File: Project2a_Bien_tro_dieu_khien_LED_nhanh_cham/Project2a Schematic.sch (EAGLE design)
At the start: 16 parts, among them U1 ARDUINOR3-BPLACE

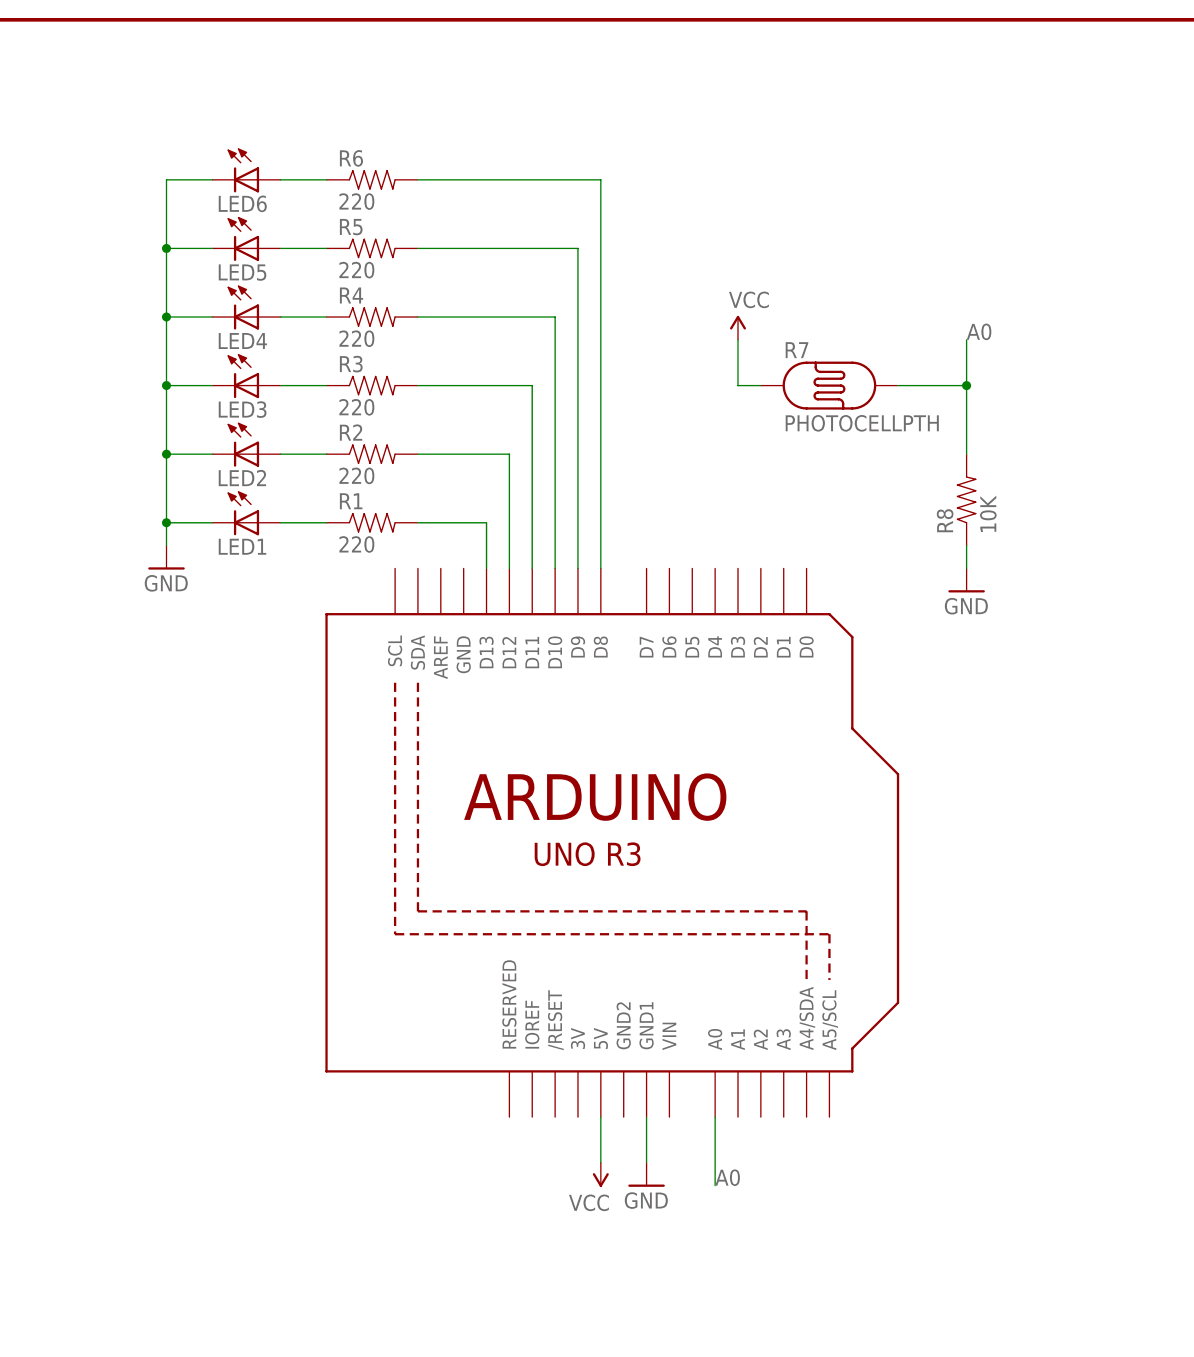
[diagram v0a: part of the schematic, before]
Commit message: Update schematic, breadboard cho nhieu projects.
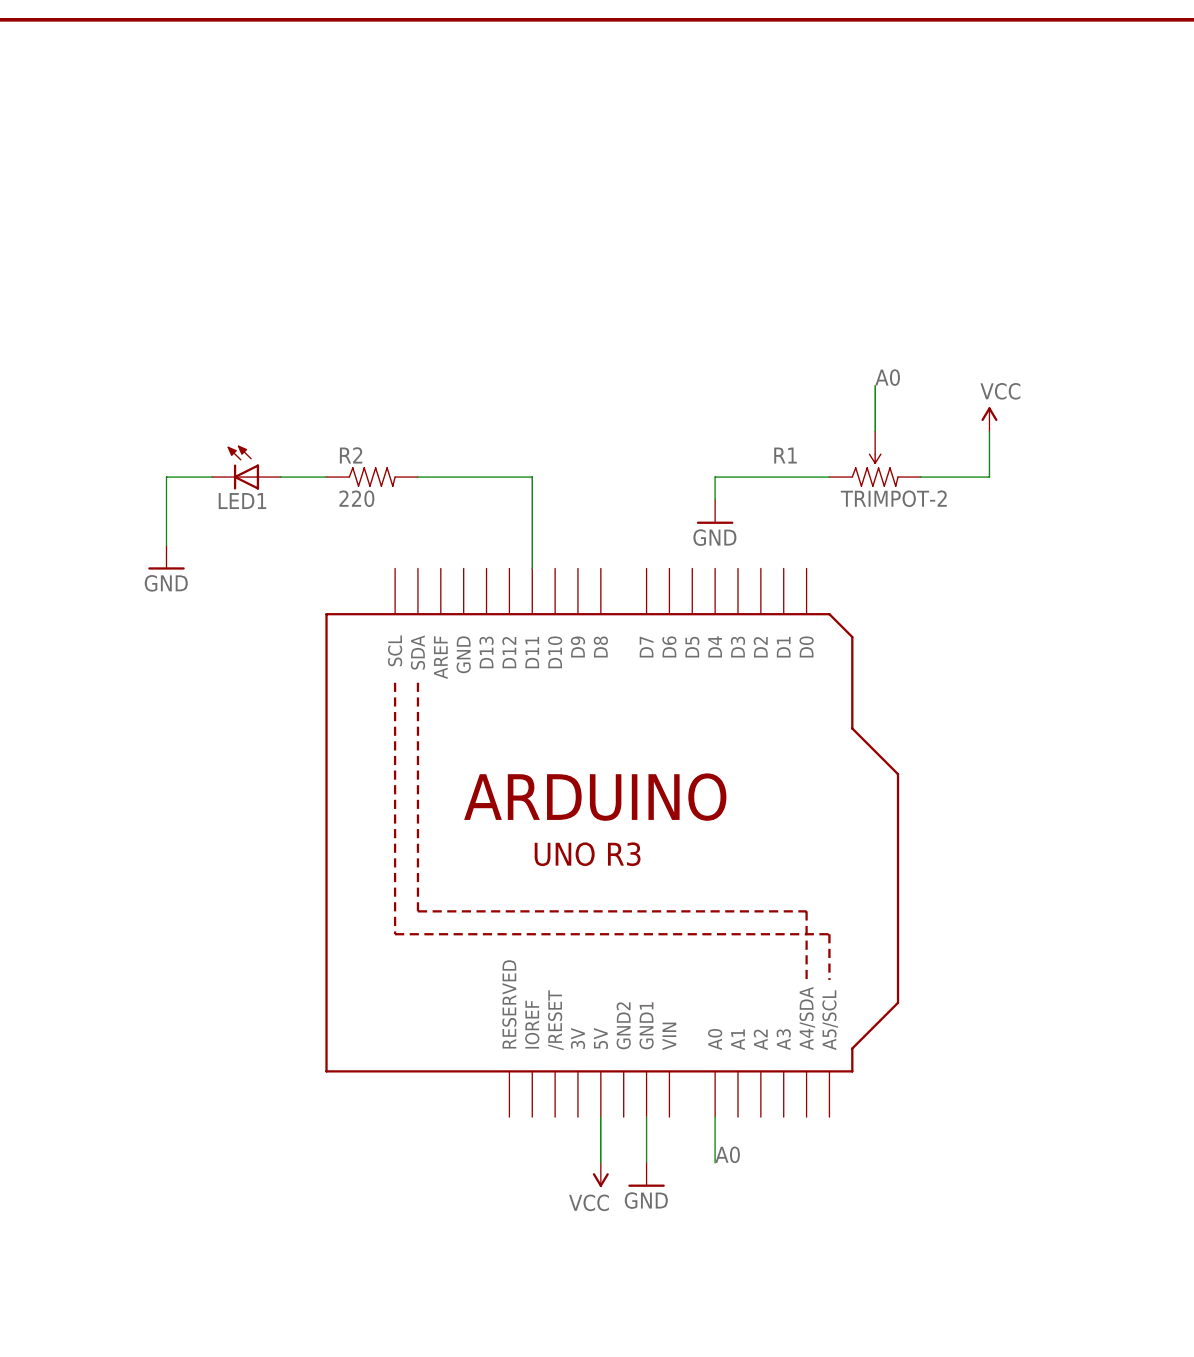
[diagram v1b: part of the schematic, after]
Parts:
- removed LED2, LED3, LED4, LED5, LED6: (no value), adafruit:LED
- removed R3, R4, R5, R6: 220, SparkFun-Passives:RESISTOR0402-RES
- removed R7: PHOTOCELLPTH, SparkFun-Sensors:PHOTOCELLPTH
- removed R8: 10K, SparkFun-Passives:RESISTOR0402-RES
- R1: value 220 -> TRIMPOT-2; device SparkFun-Passives:RESISTOR0402-RES -> SparkFun-Electromechanical:TRIMPOT-2
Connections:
- removed net N$10: LED5.A, R5.1
- removed net N$11: LED4.A, R4.1
- removed net N$12: R6.2, U1.D8
- removed net N$13: R5.2, U1.D9
- removed net N$14: R4.2, U1.D10
- removed net N$4: LED3.A, R3.1
- removed net N$5: LED2.A, R2.1
- removed net N$6: R3.2, U1.D11
- removed net N$7: R2.2, U1.D12
- removed net N$9: LED6.A, R6.1
- net A0: now also R1.WIPER; no longer R7.P$2, R8.2
- net GND: now also R1.CCW; no longer LED2.C, LED3.C, LED4.C, LED5.C, LED6.C, R8.1
- net N$1: now also R2.2, U1.D11; no longer R1.2, U1.D13
- net N$2: now also R2.1; no longer R1.1
- net VCC: now also R1.CW; no longer R7.P$1
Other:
- moved on the sheet: LED1, R2

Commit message: Thay doi schematic cua projects.
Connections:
- net A0 renamed N$3
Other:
- moved on the sheet: R1
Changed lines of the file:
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@@
 <?xml version="1.0" encoding="utf-8"?>
 <!DOCTYPE eagle SYSTEM "eagle.dtd">
-<eagle version="7.2.0">
+<eagle version="7.3.0">
 <drawing>
 <settings>
@@
 <setting verticaltext="up"/>
 </settings>
-<grid distance="0.1" unitdist="inch" unit="inch" style="dots" multiple="1" display="yes" altdistance="0.01" altunitdist="inch" altunit="inch"/>
+<grid distance="0.1" unitdist="inch" unit="inch" style="lines" multiple="1" display="yes" altdistance="0.01" altunitdist="inch" altunit="inch"/>
 <layers>
 <layer number="1" name="Top" color="4" fill="1" visible="no" active="no"/>
@@
 <instance part="LED1" gate="G$1" x="38.1" y="119.38" rot="R270"/>
 <instance part="GND2" gate="1" x="27.94" y="109.22"/>
-<instance part="GND3" gate="1" x="88.9" y="114.3"/>
-<instance part="SUPPLY2" gate="G$1" x="119.38" y="124.46"/>
+<instance part="GND3" gate="1" x="88.9" y="30.48"/>
+<instance part="SUPPLY2" gate="G$1" x="119.38" y="40.64"/>
 <instance part="FRAME1" gate="G$1" x="-33.02" y="-15.24"/>
 <instance part="FRAME1" gate="V" x="114.3" y="-15.24"/>
-<instance part="R1" gate="R?" x="106.68" y="119.38"/>
+<instance part="R1" gate="R?" x="106.68" y="35.56"/>
 </instances>
 <busses>
@@
 <segment>
 <pinref part="R1" gate="R?" pin="CW"/>
-<wire x1="111.76" y1="119.38" x2="119.38" y2="119.38" width="0.1524" layer="91"/>
+<wire x1="111.76" y1="35.56" x2="119.38" y2="35.56" width="0.1524" layer="91"/>
 <pinref part="SUPPLY2" gate="G$1" pin="VCC"/>
-<wire x1="119.38" y1="119.38" x2="119.38" y2="124.46" width="0.1524" layer="91"/>
+<wire x1="119.38" y1="35.56" x2="119.38" y2="40.64" width="0.1524" layer="91"/>
 </segment>
 </net>
@@
 <segment>
 <pinref part="GND3" gate="1" pin="GND"/>
-<wire x1="88.9" y1="116.84" x2="88.9" y2="119.38" width="0.1524" layer="91"/>
+<wire x1="88.9" y1="33.02" x2="88.9" y2="35.56" width="0.1524" layer="91"/>
 <pinref part="R1" gate="R?" pin="CCW"/>
-<wire x1="88.9" y1="119.38" x2="101.6" y2="119.38" width="0.1524" layer="91"/>
+<wire x1="88.9" y1="35.56" x2="101.6" y2="35.56" width="0.1524" layer="91"/>
 </segment>
 </net>
@@
 <pinref part="LED1" gate="G$1" pin="A"/>
 <wire x1="45.72" y1="119.38" x2="40.64" y2="119.38" width="0.1524" layer="91"/>
-</segment>
-</net>
-<net name="A0" class="0">
-<segment>
-<pinref part="R1" gate="R?" pin="WIPER"/>
-<wire x1="106.68" y1="124.46" x2="106.68" y2="129.54" width="0.1524" layer="91"/>
-<label x="106.68" y="129.54" size="1.778" layer="95"/>
-</segment>
-<segment>
-<pinref part="U1" gate="G$1" pin="A0"/>
-<wire x1="88.9" y1="48.26" x2="88.9" y2="43.18" width="0.1524" layer="91"/>
-<label x="88.9" y="43.18" size="1.778" layer="95"/>
 </segment>
 </net>
@@
 </segment>
 </net>
+<net name="N$3" class="0">
+<segment>
+<pinref part="U1" gate="G$1" pin="A0"/>
+<wire x1="88.9" y1="48.26" x2="88.9" y2="43.18" width="0.1524" layer="91"/>
+<pinref part="R1" gate="R?" pin="WIPER"/>
+<wire x1="88.9" y1="43.18" x2="106.68" y2="43.18" width="0.1524" layer="91"/>
+<wire x1="106.68" y1="43.18" x2="106.68" y2="40.64" width="0.1524" layer="91"/>
+</segment>
+</net>
